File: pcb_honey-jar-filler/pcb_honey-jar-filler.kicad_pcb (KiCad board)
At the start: 2 copper layers, 129 x 96 mm, 105 parts, among them J1 12V, J10 GPIO19, J11 GPIO23, J12 MOS2 out (FWD, Drain), J13 230V Heater, J14 5V, J15 5V, J16 GPIO15, J17 GND, J18 GND, J19 Servo, J2 12V, J20 Conn_01x07_Pin, J23 LED1, J27 Supply, J28 Relay fallback, J29 LED2, J3 3V3, J30 OLED, J31 rotary-encoder, J4 reserve Buttons, J5 4...7V, J6 Pos-switch, J7 Load-cell (HX711 input), J8 MOS1 out (FWD, Drain), K6 Relay_LEG-xxF, K7 Relay_LEG-xxF, M2 DC-worm-gear motor (Carousell), Q1 IRLB8721PBF, Q2 IRLB8721PBF, Q6 IRF5305, U1 esp32-devkit-v1_30Pin, U10 LM2576T-ADJ, U3 ULN2003, U4 HX711_24-bit-ADC_weight-scale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, U9 LM2576T-5

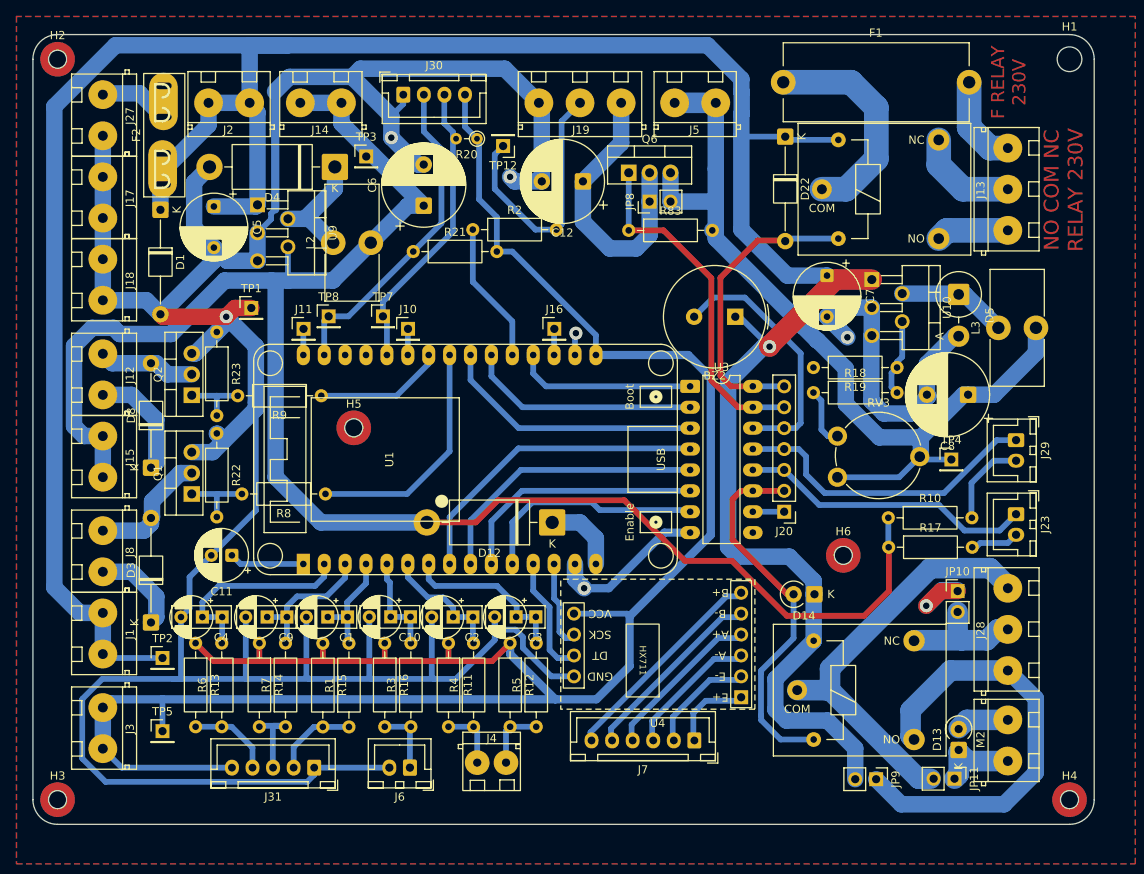
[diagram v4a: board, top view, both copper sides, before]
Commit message: pcb: Fix invalid text
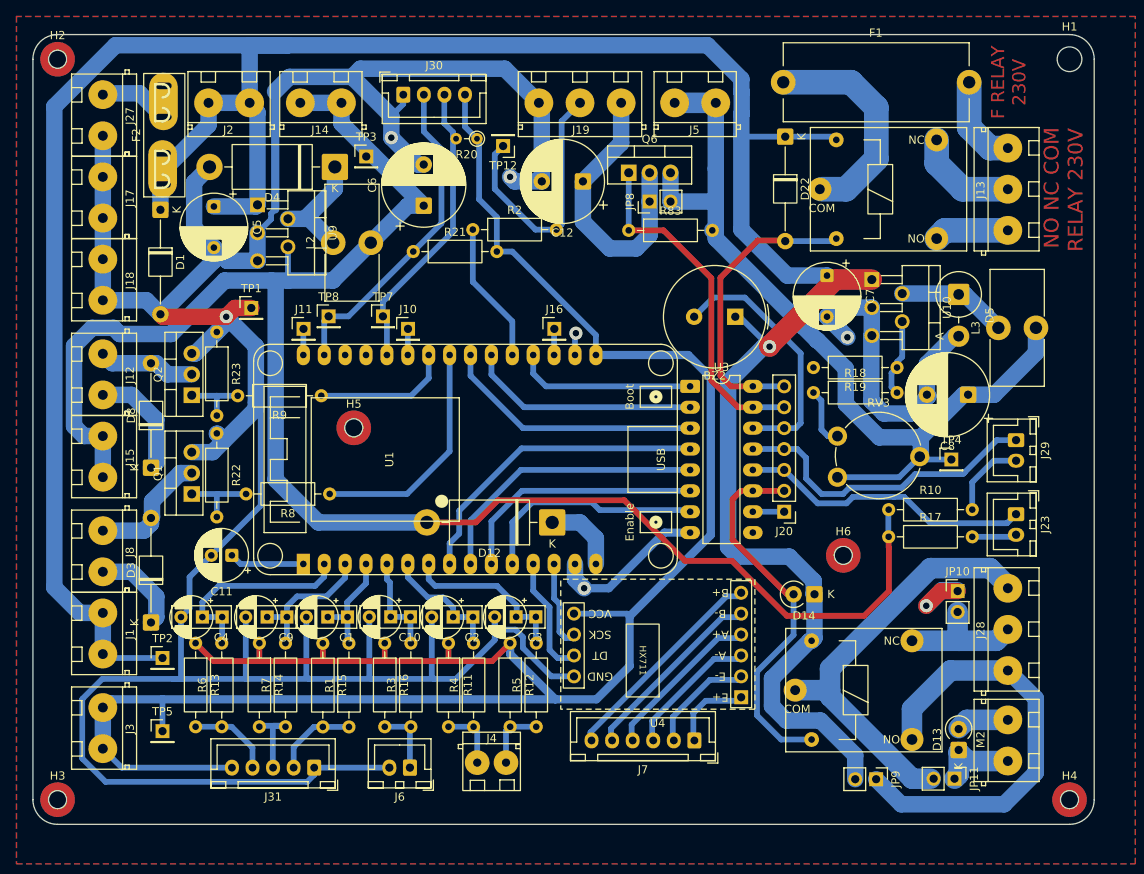
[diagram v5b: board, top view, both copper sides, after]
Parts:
- moved R17 1.27 mm to (120.0, 79.2)
- moved R10 0.99 mm to (120.0, 75.9)
- moved R8 0.51 mm to (52.1, 74.0)
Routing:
- net +5V: track 213.6 -> 214.8 mm
- net Net-(J29-Pin_2): track 10.8 -> 9.74 mm
- net /GPIO_MOS-reserve: track 15.7 -> 16.8 mm
- net Net-(J23-Pin_2): track 5.95 -> 5.43 mm
- net /GPIO_MOS-valve: track 28.9 -> 28.4 mm
- net Net-(Q1-G): track 8.94 -> 9.45 mm
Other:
- board text added: "3x EN-Mot"
- board text added: "NO NC COM"
- board text removed: "NO COM NC"

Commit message: pcb: Arrange fab text, Annotate for soldering, Fix "PWM" text
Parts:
- K6, K7: value Relay_LEG-xxF -> Relay_LEG-12
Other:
- board text added: "Changelog since tag {dblquote}pcb/v1.0-milled{dblquote} - Fixed {dblquote}PWM{dblquote} text placed over pad - Remove excess {dblquote}5V{dblquote} text"
- board text added: "Layer User7: - Marked pads to solder on top side as well: - Vias:"

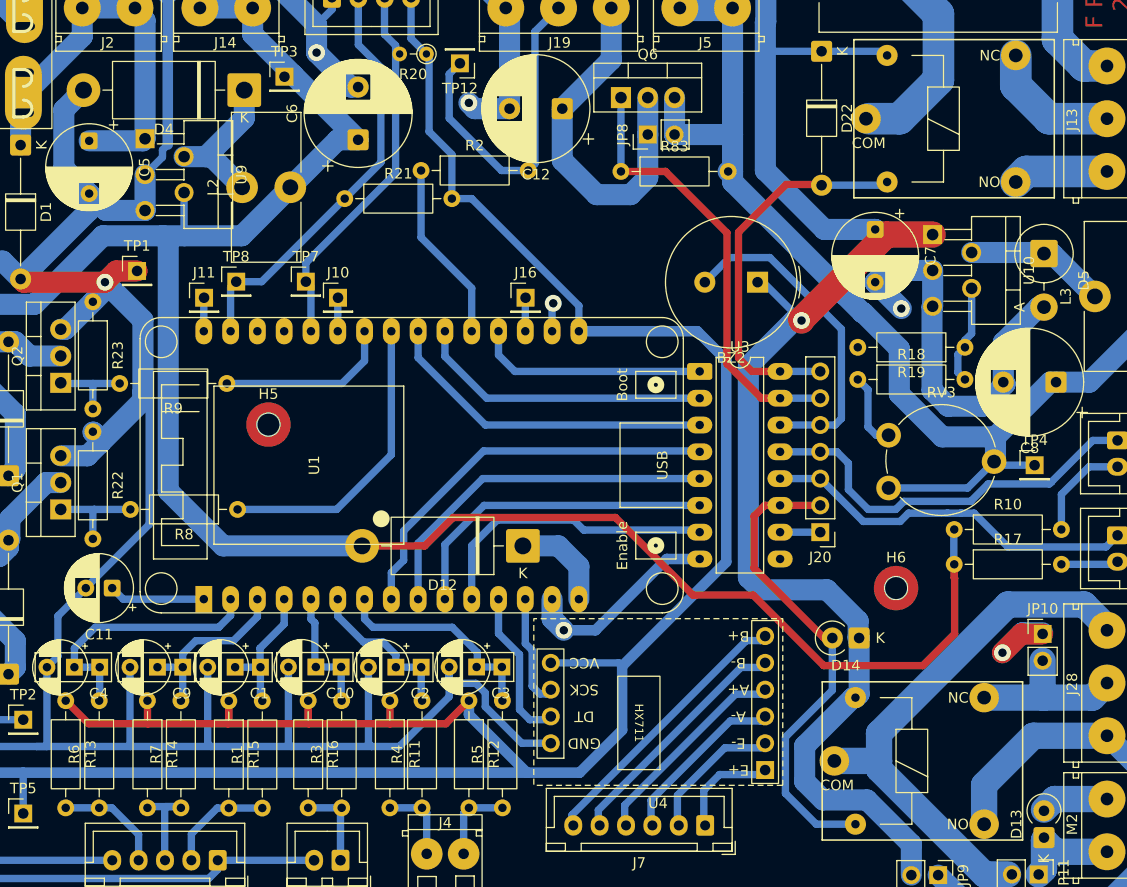
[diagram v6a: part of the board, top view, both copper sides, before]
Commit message: pcb: Update actually soldered filter R values (use sub-sheet parameters)
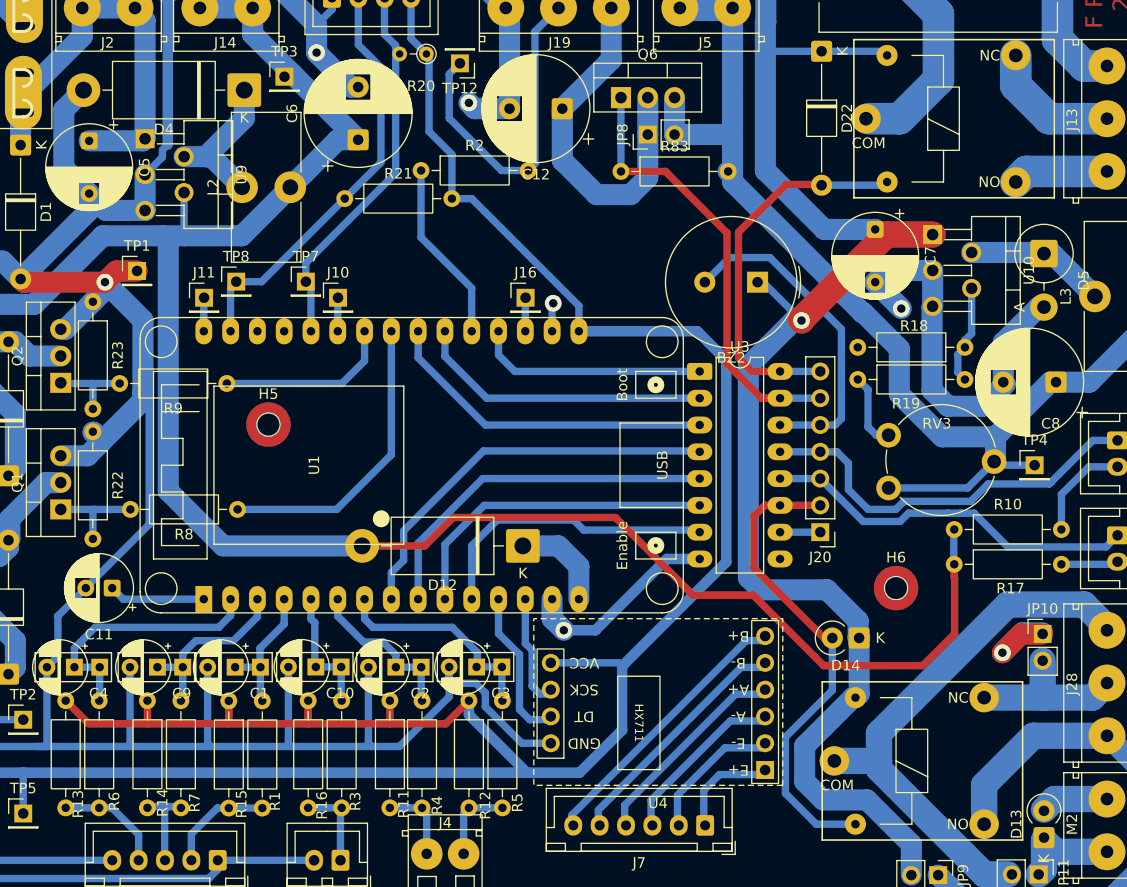
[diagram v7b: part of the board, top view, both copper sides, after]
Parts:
- C1, C4, C9: value 100n -> \100n
- C10, C2, C3: value 100n -> \10u
- R1: value 4k7 -> \2k2
- R11, R12, R15, R16: value 10k -> \10k
- R13, R14: value 10k -> \nopop
- R3, R4, R5, R6, R7: value 4k7 -> \1k
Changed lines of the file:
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@@
 		)
 	)
+	(property "C_filter" "100n")
+	(property "R_pullup" "10k")
+	(property "R_series" "2k2")
 	(net 0 "")
 	(net 1 "/OD_Buzzer")
@@
 			)
 		)
-		(property "Value" "100n"
+		(property "Value" "\\100n"
 			(at 0.3 2.2 0)
 			(layer "F.Fab")
@@
 			)
 		)
-		(property "Value" "100n"
+		(property "Value" "\\100n"
 			(at 0.3 2.2 0)
 			(layer "F.Fab")
@@
 		)
 		(property "Value" "47k"
-			(at 5.08 0 0)
+			(at 6.449 -0.217 0)
 			(layer "F.Fab")
 			(effects
@@
 		(tags "Resistor Axial_DIN0207 series Axial Horizontal pin pitch 10.16mm 0.25W = 1/4W length 6.3mm diameter 2.5mm")
 		(property "Reference" "R12"
-			(at 5.08 -2.37 90)
+			(at 9.933 -1.56 90)
 			(layer "F.SilkS")
 			(effects
@@
 			)
 		)
-		(property "Value" "10k"
+		(property "Value" "\\10k"
 			(at 5.08 0 90)
 			(layer "F.Fab")
@@
 			)
 		)
-		(property "Value" "100n"
+		(property "Value" "\\10u"
 			(at 0.3 2.2 0)
 			(layer "F.Fab")
@@
 		)
 		(property "Value" "1000u"
-			(at 2.678 2.413 90)
+			(at 1.662 1.143 180)
 			(layer "F.Fab")
 			(effects
@@
 		(tags "Resistor Axial_DIN0207 series Axial Horizontal pin pitch 10.16mm 0.25W = 1/4W length 6.3mm diameter 2.5mm")
 		(property "Reference" "R18"
-			(at 5.08 -2.37 0)
+			(at 5.334 -5.08 0)
 			(layer "F.SilkS")
 			(effects
@@
 		)
 		(property "Value" "Relay_LEG-12"
-			(at 0.348 2.571 0)
+			(at 0.221 4.222 0)
 			(layer "F.Fab")
 			(effects
@@
 		(tags "Resistor Axial_DIN0207 series Axial Horizontal pin pitch 10.16mm 0.25W = 1/4W length 6.3mm diameter 2.5mm")
 		(property "Reference" "R3"
-			(at 5.08 -2.37 90)
+			(at 0.608 1.306 90)
 			(layer "F.SilkS")
 			(effects
@@
 			)
 		)
-		(property "Value" "4k7"
+		(property "Value" "\\1k"
 			(at 5.08 0 90)
 			(layer "F.Fab")
@@
 		)
 		(property "Value" "100u"
-			(at 2.177651 2.186 90)
+			(at 1.542651 1.678 180)
 			(layer "F.Fab")
 			(effects
@@
 		)
 		(property "Value" "2200uF"
-			(at 2.46441 2.393242 0)
+			(at 1.57541 0.742242 90)
 			(layer "F.Fab")
 			(effects
@@
 		(tags "Resistor Axial_DIN0207 series Axial Horizontal pin pitch 10.16mm 0.25W = 1/4W length 6.3mm diameter 2.5mm")
 		(property "Reference" "R15"
-			(at 5.08 -2.37 90)
+			(at 9.787 -1.211 90)
 			(layer "F.SilkS")
 			(effects
@@
 			)
 		)
-		(property "Value" "10k"
+		(property "Value" "\\10k"
 			(at 5.08 0 90)
 			(layer "F.Fab")
@@
 			)
 		)
-		(property "Value" "100n"
+		(property "Value" "\\10u"
 			(at 0.3 2.2 0)
 			(layer "F.Fab")
@@
 		(tags "Resistor Axial_DIN0207 series Axial Horizontal pin pitch 10.16mm 0.25W = 1/4W length 6.3mm diameter 2.5mm")
 		(property "Reference" "R1"
-			(at 5.08 -2.37 90)
+			(at 0.627 1.211 90)
 			(layer "F.SilkS")
 			(effects
@@
 			)
 		)
-		(property "Value" "4k7"
+		(property "Value" "\\2k2"
 			(at 5.08 0 90)
 			(layer "F.Fab")
@@
 		(tags "Resistor Axial_DIN0207 series Axial Horizontal pin pitch 10.16mm 0.25W = 1/4W length 6.3mm diameter 2.5mm")
 		(property "Reference" "R19"
-			(at 5.08 -2.37 0)
+			(at 5.588 -5.334 0)
 			(layer "F.SilkS")
 			(effects
@@
 		(tags "Resistor Axial_DIN0207 series Axial Horizontal pin pitch 10.16mm 0.25W = 1/4W length 6.3mm diameter 2.5mm")
 		(property "Reference" "R13"
-			(at 5.08 -2.37 90)
+			(at 9.806 -1.179 90)
 			(layer "F.SilkS")
 			(effects
@@
 			)
 		)
-		(property "Value" "10k"
+		(property "Value" "\\nopop"
 			(at 5.08 0 90)
 			(layer "F.Fab")
@@
 		(tags "Resistor Axial_DIN0207 series Axial Horizontal pin pitch 10.16mm 0.25W = 1/4W length 6.3mm diameter 2.5mm")
 		(property "Reference" "R11"
-			(at 5.08 -2.37 90)
+			(at 9.806 -1.306 90)
 			(layer "F.SilkS")
 			(effects
@@
 			)
 		)
-		(property "Value" "10k"
+		(property "Value" "\\10k"
 			(at 5.08 0 90)
 			(layer "F.Fab")
@@
 		(tags "Resistor Axial_DIN0207 series Axial Horizontal pin pitch 10.16mm 0.25W = 1/4W length 6.3mm diameter 2.5mm")
 		(property "Reference" "R5"
-			(at 5.08 -2.37 90)
+			(at 0.481 1.433 90)
 			(layer "F.SilkS")
 			(effects
@@
 			)
 		)
-		(property "Value" "4k7"
+		(property "Value" "\\1k"
 			(at 5.08 0 90)
 			(layer "F.Fab")
@@
 			)
 		)
-		(property "Value" "100n"
+		(property "Value" "\\100n"
 			(at 0.3 2.2 0)
 			(layer "F.Fab")
@@
 		(tags "Resistor Axial_DIN0207 series Axial Horizontal pin pitch 10.16mm 0.25W = 1/4W length 6.3mm diameter 2.5mm")
 		(property "Reference" "R7"
-			(at 5.08 -2.37 90)
+			(at 0.481 1.306 90)
 			(layer "F.SilkS")
 			(effects
@@
 			)
 		)
-		(property "Value" "4k7"
+		(property "Value" "\\1k"
 			(at 5.08 0 90)
 			(layer "F.Fab")
@@
 		(tags "Potentiometer vertical Piher PT-10-V10")
 		(property "Reference" "RV3"
-			(at 5 -9.05 0)
+			(at 4.572 -6.096 0)
 			(layer "F.SilkS")
 			(effects
@@
 		)
 		(property "Value" "Relay_LEG-12"
-			(at 0.015 2.37 0)
+			(at 0.015 4.021 0)
 			(layer "F.Fab")
 			(effects
@@
 		(tags "Resistor Axial_DIN0207 series Axial Horizontal pin pitch 10.16mm 0.25W = 1/4W length 6.3mm diameter 2.5mm")
 		(property "Reference" "R4"
-			(at 5.08 -2.37 90)
+			(at 0.227 1.433 90)
 			(layer "F.SilkS")
 			(effects
@@
 			)
 		)
-		(property "Value" "4k7"
+		(property "Value" "\\1k"
 			(at 5.08 0 90)
 			(layer "F.Fab")
@@
 		(tags "Resistor Axial_DIN0207 series Axial Horizontal pin pitch 10.16mm 0.25W = 1/4W length 6.3mm diameter 2.5mm")
 		(property "Reference" "R17"
-			(at 5.08 -2.37 0)
+			(at 5.334 2.286 0)
 			(layer "F.SilkS")
 			(effects
@@
 		(tags "Resistor Axial_DIN0207 series Axial Horizontal pin pitch 10.16mm 0.25W = 1/4W length 6.3mm diameter 2.5mm")
 		(property "Reference" "R6"
-			(at 5.08 -2.37 90)
+			(at 0.608 1.433 90)
 			(layer "F.SilkS")
 			(effects
@@
 			)
 		)
-		(property "Value" "4k7"
+		(property "Value" "\\1k"
 			(at 5.08 0 90)
 			(layer "F.Fab")
@@
 		(tags "Resistor Axial_DIN0207 series Axial Horizontal pin pitch 10.16mm 0.25W = 1/4W length 6.3mm diameter 2.5mm")
 		(property "Reference" "R16"
-			(at 5.08 -2.37 90)
+			(at 9.933 -1.306 90)
 			(layer "F.SilkS")
 			(effects
@@
 			)
 		)
-		(property "Value" "10k"
+		(property "Value" "\\10k"
 			(at 5.08 0 90)
 			(layer "F.Fab")
@@
 		)
 		(property "Value" "100u"
-			(at 2.032 2.032 90)
+			(at -0.254 5.08 180)
 			(layer "F.Fab")
 			(effects
@@
 		(tags "Resistor Axial_DIN0207 series Axial Horizontal pin pitch 10.16mm 0.25W = 1/4W length 6.3mm diameter 2.5mm")
 		(property "Reference" "R14"
-			(at 5.08 -2.37 90)
+			(at 9.679 -1.433 90)
 			(layer "F.SilkS")
 			(effects
@@
 			)
 		)
-		(property "Value" "10k"
+		(property "Value" "\\nopop"
 			(at 5.08 0 90)
 			(layer "F.Fab")
@@
 		(tags "Resistor Axial_DIN0204 series Axial Vertical pin pitch 2.54mm 0.167W length 3.6mm diameter 1.6mm")
 		(property "Reference" "R20"
-			(at 1.27 -1.92 0)
+			(at 0.508 -3.048 0)
 			(layer "F.SilkS")
 			(effects
@@
 			)
 		)
-		(property "Value" "100n"
+		(property "Value" "\\10u"
 			(at 0.3 2.2 0)
 			(layer "F.Fab")
@@
 		(tags "CP Radial series Radial pin pitch 5.00mm diameter 10mm height 16mm Electrolytic Capacitor")
 		(property "Reference" "C8"
-			(at 2.5 -6.25 0)
+			(at 0.508 -3.937 0)
 			(layer "F.SilkS")
 			(effects
@@
 		)
 		(property "Value" "1000u"
-			(at 2.286 2.54 0)
+			(at 1.651 0 90)
 			(layer "F.Fab")
 			(effects
@@
 			(layer "F.Fab")
 		)
-		(fp_text user "${REFERENCE}"
-			(at 2.5 0 0)
-			(layer "F.Fab")
-			(effects
-				(font
-					(size 1 1)
-					(thickness 0.15)
-				)
-			)
-		)
 		(pad "1" thru_hole roundrect

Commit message: Fix crash on nvs-write: Change H711 DT-pin (non strapping), Add notes to schematic + pcb
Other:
- board text added: "TODO next version: - Reroute H711 DT pin (currently jump wired to GPIO19)"
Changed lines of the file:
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@@
+		)
+	)
+	(gr_text "TODO next version:\n  - Reroute H711 DT pin (currently jump wired to GPIO19)"
+		(at 163.4 59.8 0)
+		(layer "Cmts.User")
+		(effects
+			(font
+				(size 2 2)
+				(thickness 0.4)
+				(bold yes)
+			)
+			(justify left top)
 		)
 	)
